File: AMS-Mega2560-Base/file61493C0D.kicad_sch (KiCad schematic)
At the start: 50 parts, among them IC10 LM2597MX-ADJ_NOPB, IC11 LM2597M-3.3_NOPB, IC12 OPA2340PA, IC9 LM2670SX-5.0_NOPB, J21 Screw_Terminal_01x03, J22 Conn_01x07, Q21 IRF9Z34NPBF, Q22 IRF9610PBF-BE3, Q23 2N7000, Q5 2N7000, Q6 IRF9Z34NPBF, U1 BK_HTC-15M, U2 TL431LP

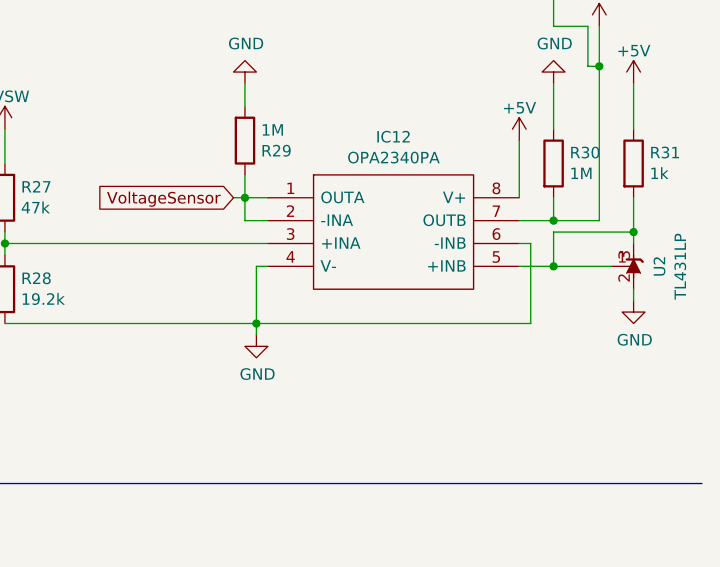
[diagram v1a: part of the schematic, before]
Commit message: fixed 2.5v source. added gnd fill area to keep the noise down.
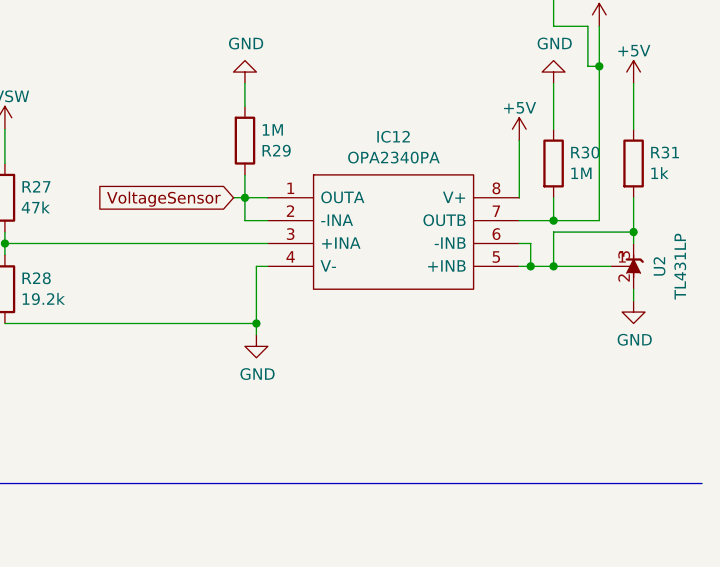
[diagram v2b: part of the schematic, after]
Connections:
- net GND: no longer IC12.6 (-INB)
- net at IC12.5 (+INB), R31.2, U2.1 (REF)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: now also IC12.6 (-INB)
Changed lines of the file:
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@@
   (junction (at 135.89 48.26) (diameter 0) (color 0 0 0 0)
+  )
+  (junction (at 265.43 69.85) (diameter 0) (color 0 0 0 0)
   )
   (junction (at 49.53 132.715) (diameter 0) (color 0 0 0 0)
@@
     (stroke (width 0) (type default) (color 0 0 0 0))
   )
+  (wire (pts (xy 265.43 69.85) (xy 267.97 69.85))
+    (stroke (width 0) (type default) (color 0 0 0 0))
+  )
   (wire (pts (xy 102.87 50.8) (xy 102.87 54.61))
     (stroke (width 0) (type default) (color 0 0 0 0))
@@
     (stroke (width 0) (type default) (color 0 0 0 0))
   )
-  (wire (pts (xy 265.43 76.2) (xy 265.43 67.31))
-    (stroke (width 0) (type default) (color 0 0 0 0))
-  )
   (wire (pts (xy 241.3 146.05) (xy 241.3 142.24))
     (stroke (width 0) (type default) (color 0 0 0 0))
@@
     (stroke (width 0) (type default) (color 0 0 0 0))
   )
-  (wire (pts (xy 264.16 69.85) (xy 267.97 69.85))
+  (wire (pts (xy 264.16 69.85) (xy 265.43 69.85))
     (stroke (width 0) (type default) (color 0 0 0 0))
   )
@@
     (stroke (width 0) (type default) (color 0 0 0 0))
   )
-  (wire (pts (xy 234.95 76.2) (xy 265.43 76.2))
-    (stroke (width 0) (type default) (color 0 0 0 0))
-  )
   (wire (pts (xy 72.39 63.5) (xy 77.47 63.5))
     (stroke (width 0) (type default) (color 0 0 0 0))
@@
     (stroke (width 0) (type default) (color 0 0 0 0))
   )
+  (wire (pts (xy 265.43 67.31) (xy 265.43 69.85))
+    (stroke (width 0) (type default) (color 0 0 0 0))
+  )

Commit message: ready to autoroute
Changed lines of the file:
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@@
   (junction (at 233.68 62.23) (diameter 0) (color 0 0 0 0)
-  )
-  (junction (at 175.26 48.26) (diameter 0) (color 0 0 0 0)
   )
   (junction (at 247.65 142.24) (diameter 0) (color 0 0 0 0)
@@
     (stroke (width 0) (type default) (color 0 0 0 0))
   )
-  (wire (pts (xy 175.26 48.26) (xy 135.89 48.26))
-    (stroke (width 0) (type default) (color 0 0 0 0))
-  )
   (wire (pts (xy 111.76 48.26) (xy 100.33 48.26))
     (stroke (width 0) (type default) (color 0 0 0 0))
@@
     (stroke (width 0) (type default) (color 0 0 0 0))
   )
-  (wire (pts (xy 191.77 48.26) (xy 175.26 48.26))
+  (wire (pts (xy 135.89 48.26) (xy 191.77 48.26))
     (stroke (width 0) (type default) (color 0 0 0 0))
   )
@@
       (effects (font (size 1.27 1.27)) hide)
     )
-    (pin "1")
-  )
-  (symbol (lib_id "power:PWR_FLAG") (at 175.26 48.26 0) (unit 1)
-    (in_bom yes) (on_board yes) (fields_autoplaced)
-    (property "Reference" "#FLG07" (id 0) (at 175.26 46.355 0)
-      (effects (font (size 1.27 1.27)) hide)
-    )
-    (property "Value" "PWR_FLAG" (id 1) (at 175.26 44.6555 0))
-    (property "Footprint" "" (id 2) (at 175.26 48.26 0)
-      (effects (font (size 1.27 1.27)) hide)
-    )
-    (property "Datasheet" "~" (id 3) (at 175.26 48.26 0)
-      (effects (font (size 1.27 1.27)) hide)
-    )

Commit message: working on this.
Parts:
- removed C13, C14: 15uF, Capacitor_THT:CP_Radial_D5.0mm_P2.50mm, symbol Device:CP
- removed C15, C17, C20, C21, C24: 0.1uF, Capacitor_THT:C_Rect_L9.0mm_W3.6mm_P7.50mm_MKT, symbol Device:C
- removed C16: 0.47uF, Capacitor_THT:C_Rect_L9.0mm_W3.6mm_P7.50mm_MKT, symbol Device:C
- removed C18, C23, C26: 120uF, Capacitor_THT:CP_Radial_D8.0mm_P5.00mm, symbol Device:CP
- removed C19: 3.3nF, Capacitor_THT:C_Rect_L9.0mm_W3.6mm_P7.50mm_MKT, symbol Device:C
- removed C22, C25: 68uF, Capacitor_THT:CP_Radial_D5.0mm_P2.50mm, symbol Device:CP
- removed D1: 1N4007, Diode_THT:D_DO-41_SOD81_P10.16mm_Horizontal, symbol Diode:1N4007
- removed D6: SR305-TP, SamacSys_Parts:DIOAD2860W130L840D505, symbol SamacSys_Parts:SR305-TP
- removed D7, D8: 1N5817, SamacSys_Parts:DIOAD1414W86L464D238, symbol SamacSys_Parts:1N5817
- removed IC10: LM2597MX-ADJ_NOPB, SamacSys_Parts:SOIC127P600X175-8N, symbol SamacSys_Parts:LM2597MX-ADJ_NOPB
- removed IC11: LM2597M-3.3_NOPB, SamacSys_Parts:SOIC127P600X175-8N, symbol SamacSys_Parts:LM2597M-3.3_NOPB
- removed IC12: OPA2340PA, SamacSys_Parts:DIP794W53P254L959H508Q8N, symbol SamacSys_Parts:OPA2340PA
- removed IC9: LM2670SX-5.0_NOPB, SamacSys_Parts:LM2670SX50NOPB, symbol SamacSys_Parts:LM2670SX-5.0_NOPB
- removed J22: Conn_01x07, Connector_PinHeader_2.54mm:PinHeader_1x07_P2.54mm_Vertical, symbol Connector_Generic:Conn_01x07
- removed L1: 33mH, Inductor_THT:L_Axial_L9.5mm_D4.0mm_P15.24mm_Horizontal_Fastron_SMCC, symbol Device:L
- removed L2, L3: 100mH, Inductor_THT:L_Axial_L9.5mm_D4.0mm_P15.24mm_Horizontal_Fastron_SMCC, symbol Device:L
- removed Q21: IRF9Z34NPBF, SamacSys_Parts:TO254P469X1042X1967-3P, symbol SamacSys_Parts:IRF9Z34NPBF
- removed Q22: IRF9610PBF-BE3, TO254P465X1024X2050-3P, symbol Samac_Sys:IRF9610PBF-BE3
- removed Q23, Q5: 2N7000, Package_TO_SOT_THT:TO-92_Inline, symbol Transistor_FET:2N7000
- removed R12, R29, R30, R63: 1M, Resistor_THT:R_Axial_DIN0207_L6.3mm_D2.5mm_P2.54mm_Vertical, symbol Device:R
- removed R22, R23, R26: 4.7K, Resistor_THT:R_Axial_DIN0207_L6.3mm_D2.5mm_P2.54mm_Vertical, symbol Device:R
- removed R24, R31: 1k, Resistor_THT:R_Axial_DIN0207_L6.3mm_D2.5mm_P2.54mm_Vertical, symbol Device:R
- removed R25: 7.5K, Resistor_THT:R_Axial_DIN0207_L6.3mm_D2.5mm_P2.54mm_Vertical, symbol Device:R
- removed R27: 47k, Resistor_THT:R_Axial_DIN0207_L6.3mm_D2.5mm_P2.54mm_Vertical, symbol Device:R
- removed R28: 19.2k, Resistor_THT:R_Axial_DIN0207_L6.3mm_D2.5mm_P2.54mm_Vertical, symbol Device:R
- removed R61: 10k, Resistor_THT:R_Axial_DIN0207_L6.3mm_D2.5mm_P2.54mm_Vertical, symbol Device:R
- removed R62: 100k, Resistor_THT:R_Axial_DIN0207_L6.3mm_D2.5mm_P2.54mm_Vertical, symbol Device:R
- removed U2: TL431LP, Package_TO_SOT_THT:TO-92_Inline, symbol Reference_Voltage:TL431LP
- removed Z8: BZX79C10, SamacSys_Parts:DIOAD1068W53L380D172, symbol SamacSys_Parts:BZX79C10
- added J1: Conn_01x03, Connector_PinHeader_2.54mm:PinHeader_1x03_P2.54mm_Vertical, symbol Connector_Generic:Conn_01x03
- added Q15: 2N7000, Package_TO_SOT_THT:TO-92_Inline, symbol Transistor_FET:2N7000
- added Q17: IRF9Z34NPBF, SamacSys_Parts:TO254P469X1042X1967-3P, symbol SamacSys_Parts:IRF9Z34NPBF
- added R51, R53: 100k, Resistor_THT:R_Axial_DIN0207_L6.3mm_D2.5mm_P2.54mm_Vertical, symbol Device:R
- added R54: 10k, Resistor_THT:R_Axial_DIN0207_L6.3mm_D2.5mm_P2.54mm_Vertical, symbol Device:R
- added Z5: BZX79C10, SamacSys_Parts:DIOAD1068W53L380D172, symbol SamacSys_Parts:BZX79C10
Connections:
- net +5V: now also J1.2 (Pin_2)
- net +VDC: now also Q17.3, R53.1, Z5.1
- net GND: now also J1.3 (Pin_3), Q15.1 (S), R51.2
- net PowerOn: now also Q15.2 (G), R51.1
- new net: Q17.1, R53.2, R54.1, Z5.2
- new net: Q15.3 (D), R54.2
- new net VPP: J1.1 (Pin_1), Q17.2
- no-connect marks 1 -> 0
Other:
- note removed: "10 Volt Regulator"
- note removed: "3.3 Volt Regulator"
- note removed: "5 Volt Regulator"
- note removed: "PowerSwitch"
- note removed: "Voltage Output Header"
- note removed: "Voltage Sensor 2.5 Ref Voltage Buffer"
